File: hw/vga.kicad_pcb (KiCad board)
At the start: 2 copper layers, 36.8 x 36.8 mm, 23 parts, among them P1 CONN_01X15, P2 COLOR_SELECT, P3 CONN_01X14, P4 CONN_01X02, P5 CLOCK_SELECT, U1 74HC4053, U2 23LCV512, U3 NB3N502, Y1 10MHz

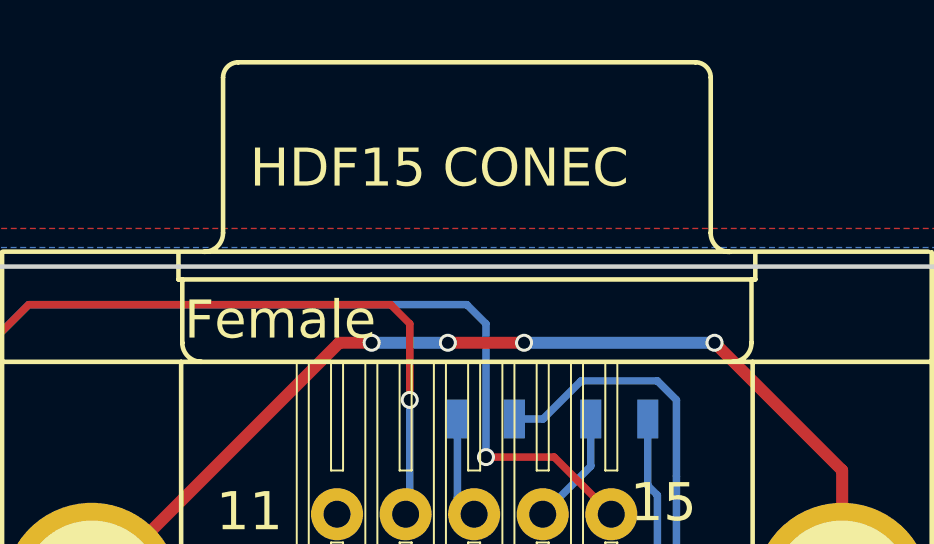
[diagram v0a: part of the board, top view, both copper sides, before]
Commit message: Upgraded project to Kicad 6
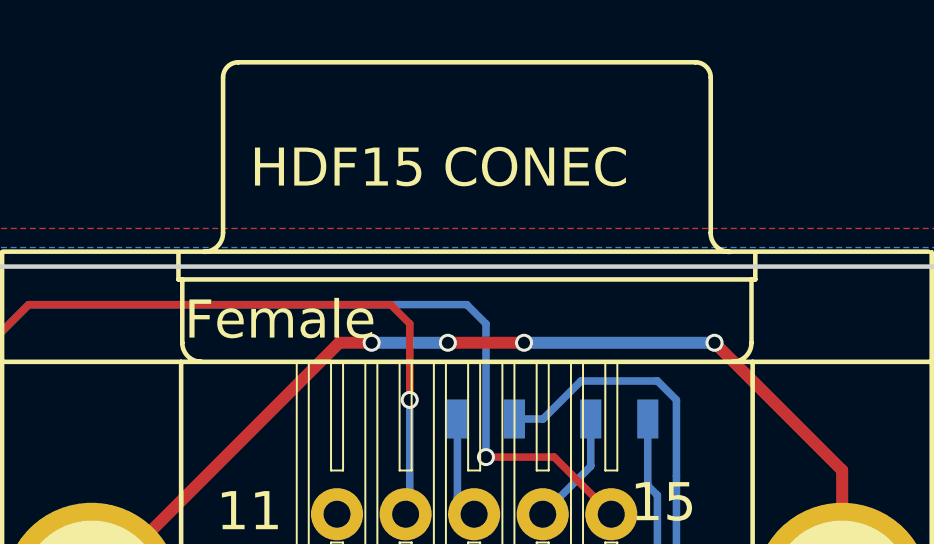
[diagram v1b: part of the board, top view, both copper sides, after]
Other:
- net class Default removed
- net class Power removed

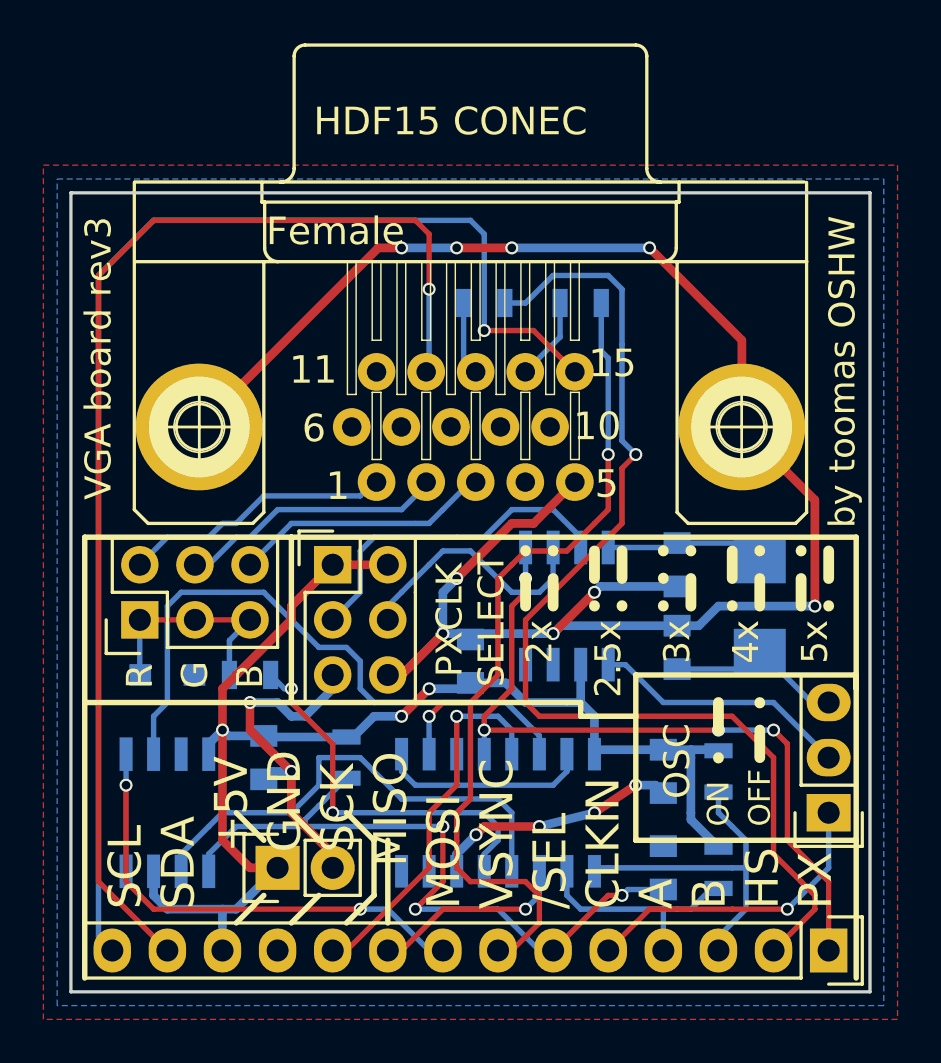
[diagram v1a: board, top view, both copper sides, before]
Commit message: Changed PLL chip to ICS501 and removed onboard oscillator option. Changed J1 footprint to 14 pin double row pin header. Swapped J1 pins 2 and 3 (hsync and B). J1 pin 1 is now ground (used to be pixel clock out). B line now has pulldown (used to be pullup). Rerouted the board for lower EMC (but still 2 layers).
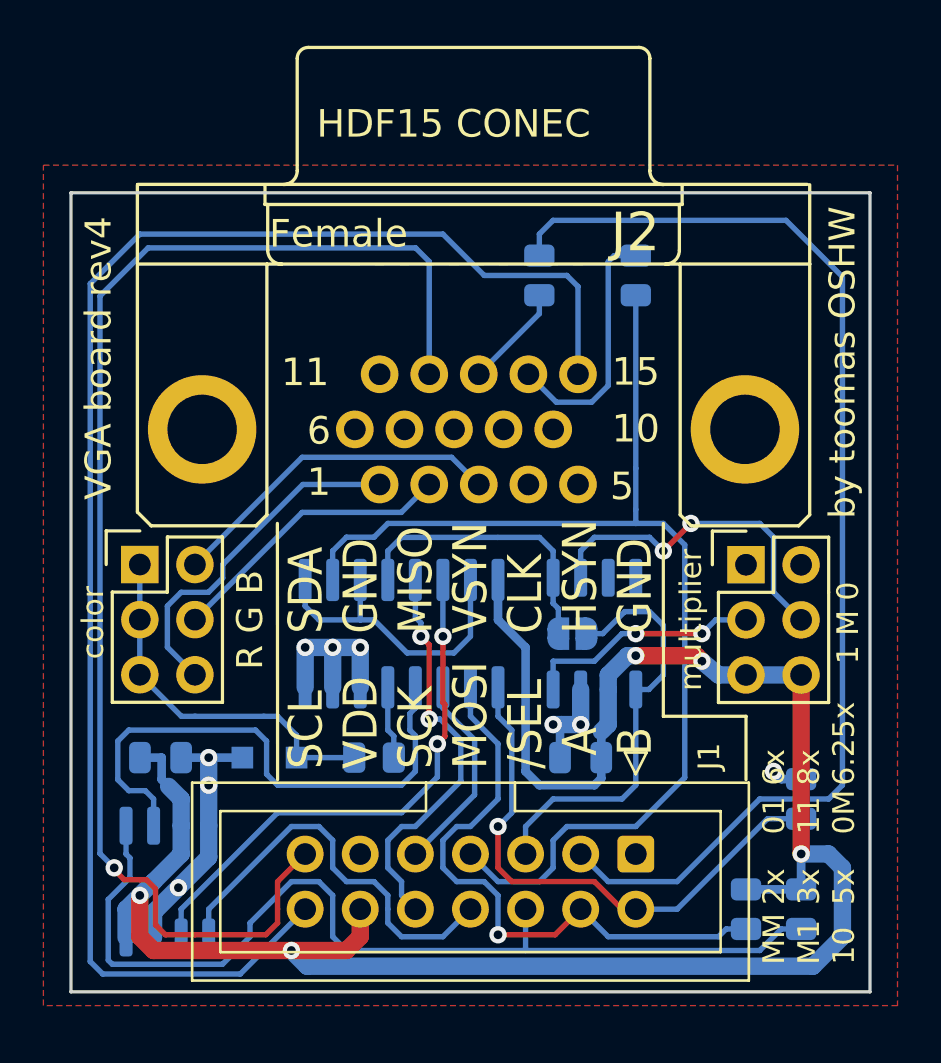
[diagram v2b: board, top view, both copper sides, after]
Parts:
- removed the C1 at (152.4, 88.3)
- removed the C2 at (161.9, 87.6)
- removed C3: 1p, Capacitors_SMD:C_0805
- removed C6: 100p, Capacitors_SMD:C_0805
- removed the JP2 at (168.9, 95.2)
- removed P1: CONN_01X15, vga:con-subd-HDF15H
- removed P3: CONN_01X14, Pin_Headers:Pin_Header_Straight_1x14
- removed P4: CONN_01X02, Pin_Headers:Pin_Header_Straight_1x02
- removed Y1: 10MHz, Crystals:Crystal_SMD_5032_2Pads
- added J1: Conn_02x07_Odd_Even, Connector_IDC:IDC-Header_2x07_P2.54mm_Vertical, F.Cu at (160.0, 97.2)
- added J2: DB15_Female_HighDensity_MountingHoles, vga:con-subd-HDF15H, F.Cu at (152.5, 77.6)
- added JP3: SolderJumper_2_Open, Jumper:SolderJumper-2_P1.3mm_Open_RoundedPad1.0x1.5mm, B.Cu at (157.1, 87.0)
- C1: renamed from C4; footprint Capacitors_SMD:C_0805 -> Capacitor_SMD:C_0805_2012Metric
- C2: renamed from C5; footprint Capacitors_SMD:C_0805 -> Capacitor_SMD:C_0805_2012Metric
- D1: footprint Diodes_SMD:SOD-323_HandSoldering -> Diode_SMD:D_SOD-323_HandSoldering
- JP1: renamed from P2; value COLOR_SELECT -> color
- JP2: renamed from P5; value CLOCK_SELECT -> multiplier
- R1: renamed from R4; value 2k2 -> 10k; footprint Resistors_SMD:R_0805 -> Resistor_SMD:R_0805_2012Metric
- R2, R3: value 2k2 -> 10k; footprint Resistors_SMD:R_0805 -> Resistor_SMD:R_0805_2012Metric
- R4: renamed from R8; footprint Resistors_SMD:R_0805 -> Resistor_SMD:R_0805_2012Metric
- R5, R6: footprint Resistors_SMD:R_0805 -> Resistor_SMD:R_0805_2012Metric
- U1: footprint Housings_SOIC:SOIC-16_3.9x9.9mm_Pitch1.27mm -> Package_SO:SOIC-16_3.9x9.9mm_P1.27mm
- U2: footprint Housings_SOIC:SOIC-8_3.9x4.9mm_Pitch1.27mm -> Package_SO:SO-8_3.9x4.9mm_P1.27mm
- U3: value NB3N502 -> ICS501; footprint Housings_SOIC:SOIC-8_3.9x4.9mm_Pitch1.27mm -> Package_SO:SO-8_3.9x4.9mm_P1.27mm
- moved R1 22.1 mm to (167.6, 99.7)
- moved JP2 19.0 mm to (165.1, 83.8)
- moved U1 9.38 mm to (149.2, 87.0)
- moved R6 6.87 mm to (148.0, 92.7)
- moved D1 6.05 mm to (143.1, 92.7), turned to 0 degrees
- moved C2 4.76 mm to (138.1, 92.7), turned to 0 degrees
- moved R2 4.02 mm to (167.6, 94.6), turned to -90 degrees
- moved C1 3.86 mm to (157.5, 92.7), turned to 180 degrees
- moved U2 3.17 mm to (138.4, 98.4), turned to -90 degrees
- moved R5 2.84 mm to (160.0, 70.5), turned to -90 degrees
- moved R4 2.84 mm to (155.6, 70.5), turned to 90 degrees
- moved JP1 2.55 mm to (137.2, 83.8), turned to 0 degrees
- moved R3 2.29 mm to (165.1, 99.7)
- moved U3 1.80 mm to (158.1, 87.0)
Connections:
- net //SEL renamed //SEL
- net /PXCLK renamed Net-(JP3-Pad2)
- JP1 pad 2: /PX_R -> /PX_B
- JP1 pad 6: /PX_B -> /PX_R
- JP2 pad 1: VDD -> GND
- JP2 pad 2: VDD -> GND
- JP2 pad 3: Net-(P5-Pad3) -> Net-(JP2-Pad3)
- JP2 pad 5: GND -> VDD
- JP2 pad 6: GND -> VDD
- R2 pad 1: /B -> GND
- R2 pad 2: VDD -> /B
- U3 pad 1: Net-(JP2-Pad2) -> /CLKIN
- U3 pad 4: Net-(U3-Pad4) -> Net-(JP2-Pad3)
- U3 pad 7: Net-(P5-Pad3) -> unconnected-(U3-Pad7)
- U3 pad 8: Net-(C3-Pad1) -> unconnected-(U3-Pad8)
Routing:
- net GND: track 108.9 -> 26.1 mm, vias 15 -> 9
- net VDD: track 66.0 -> 96.3 mm, vias 3 -> 5
- net Net-(JP3-Pad2): track 35.3 -> 13.4 mm, vias 4 -> 0
- net /A: track 10.7 -> 27.7 mm, vias 0 -> 1
- net Net-(P5-Pad3): track 16.9 -> 0.00 mm
- net /PIXEL: track 17.9 -> 3.35 mm, vias 2 -> 0
- net Net-(JP2-Pad2): track 11.9 -> 0.00 mm
- net //SEL: track 33.5 -> 45.4 mm, vias 3 -> 0
- net /SCL: track 59.9 -> 71.1 mm, vias 1 -> 0
- net Net-(JP2-Pad3): track 0.00 -> 11.0 mm, vias 0 -> 2
- net /VSYNC: track 42.1 -> 52.9 mm, vias 2 -> 0
- net /B: track 15.4 -> 25.3 mm, vias 0 -> 1
- net Net-(C2-Pad1): track 8.33 -> 0.00 mm
- net /VSYNC_OUT: track 3.84 -> 11.6 mm
- net Net-(C3-Pad1): track 7.42 -> 0.00 mm
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- removed copper zone on B.Cu, net GND
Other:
- board text added: "01 11 0M"
- board text added: "1 M 0"
- board text added: "2x 3x 5x"
- board text added: "6x 8x 6.25x"
- board text added: "MM M1 10"
- board text added: "R G B"
- board text added: "SCL VDD SCK MOSI /SEL A B"
- board text added: "SDA GND MISO VSYN CLK HSYN GND"
- board text added: "VGA board rev4"
- board text added: "color"
- board text added: "multiplier"
- board text removed: "2.5x"
- board text removed: "2x"
- board text removed: "3x"
- board text removed: "4x"
- board text removed: "5x"
- board text removed: "B"
- board text removed: "G"
- board text removed: "OFF"
- board text removed: "ON"
- board text removed: "OSC"
- board text removed: "PXCLK SELECT"
- board text removed: "R"
- board text removed: "SCL SDA +5V GND SCK MISO MOSI VSYNC /SEL CLKIN A B HS PX"
- board text removed: "VGA board rev3"

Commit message: Reduced J1 to 10pins by removing all non-essential pins. Reviewed comments on the schematic. Added solder jumper so that more PLL chips could be used. Changed AB input to use pullups like rev3 did (but with 4x higher value). Finished board layout.
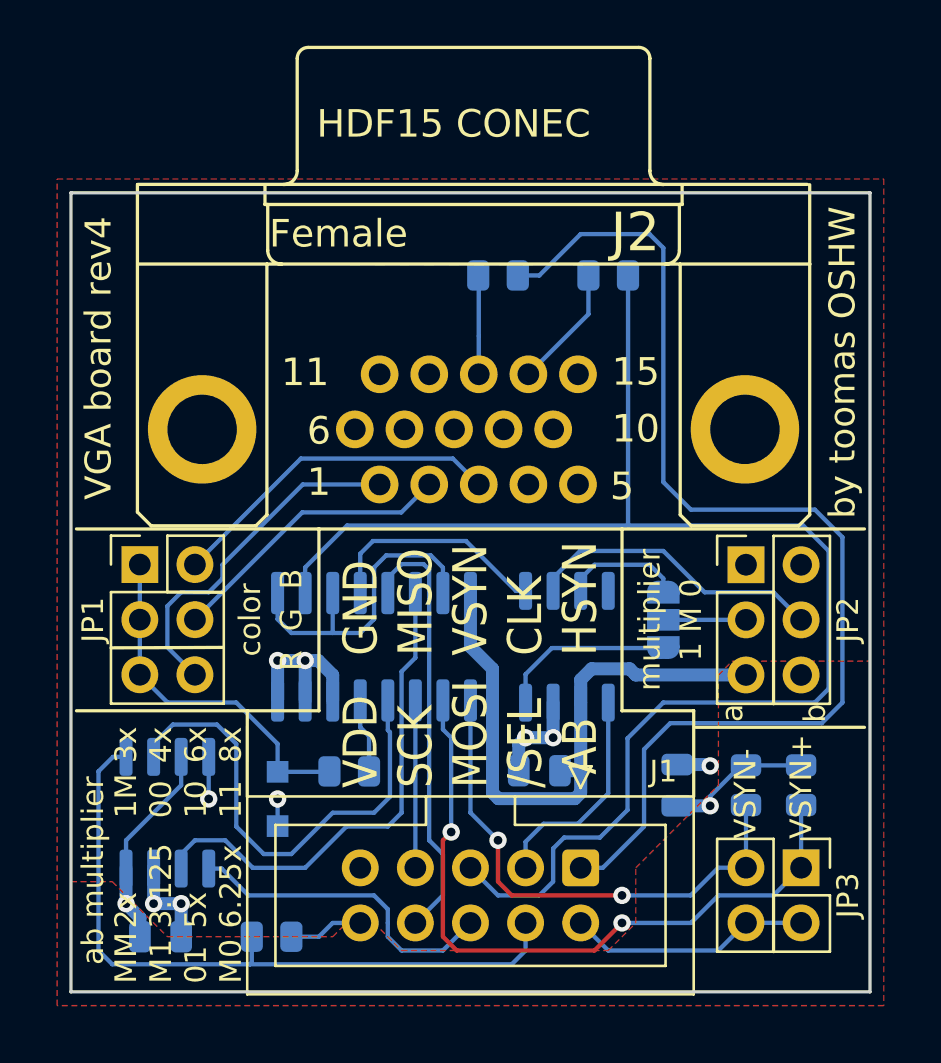
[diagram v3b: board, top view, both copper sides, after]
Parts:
- added C3: 100n, Capacitor_SMD:C_0805_2012Metric, B.Cu at (161.9, 94.0)
- added JP4: SolderJumper_3_Bridged12, Jumper:SolderJumper-3_P1.3mm_Open_RoundedPad1.0x1.5mm, B.Cu at (161.3, 86.4)
- J1: value Conn_02x07_Odd_Even -> Conn_02x05_Odd_Even; footprint Connector_IDC:IDC-Header_2x07_P2.54mm_Vertical -> Connector_IDC:IDC-Header_2x05_P2.54mm_Vertical
- JP1, JP2: footprint Pin_Headers:Pin_Header_Straight_2x03 -> Connector_PinHeader_2.54mm:PinHeader_2x03_P2.54mm_Vertical
- JP3: value SolderJumper_2_Open -> Conn_02x02_Odd_Even; footprint Jumper:SolderJumper-2_P1.3mm_Open_RoundedPad1.0x1.5mm -> Connector_PinHeader_2.54mm:PinHeader_2x02_P2.54mm_Vertical; moved to F.Cu
- moved R1 24.4 mm to (143.2, 101.0), turned to 0 degrees
- moved JP3 15.1 mm to (167.6, 97.8), turned to -90 degrees
- moved C2 8.26 mm to (138.1, 101.0)
- moved R3 5.71 mm to (165.1, 94.0), turned to -90 degrees
- moved U2 3.17 mm to (138.4, 95.2)
- moved J1 2.62 mm to (157.5, 97.8)
- moved C1 2.00 mm to (155.6, 93.3)
- moved D1 1.94 mm to (143.5, 94.6), turned to 90 degrees
- moved R4 1.91 mm to (153.7, 70.5), turned to 0 degrees
- moved U3 1.41 mm to (156.8, 87.6)
- moved U1 1.41 mm to (148.0, 87.6)
- moved R6 1.31 mm to (146.8, 93.3)
- moved R5 1.27 mm to (158.8, 70.5), turned to 0 degrees
- moved R2 0.63 mm to (167.6, 94.0)
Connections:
- net Net-(JP2-Pad4) renamed /S0_a
- J1 pad 1: GND -> /HSYNC
- J1 pad 10: /SCK -> VDD
- J1 pad 2: /B -> /AB
- J1 pad 3: /HSYNC -> /CLKIN
- J1 pad 4: /A -> //SEL
- J1 pad 5: /CLKIN -> /VSYNC
- J1 pad 6: //SEL -> /MOSI
- J1 pad 7: /VSYNC -> /MISO
- J1 pad 8: /MOSI -> /SCK
- J1 pad 9: /MISO -> GND
- J2 pad 12: /SDA -> unconnected-(J2-Pad12)
- J2 pad 15: /SCL -> unconnected-(J2-Pad15)
- JP2 pad 3: Net-(JP2-Pad3) -> /S1_b
- JP3 pad 1: /CLKIN -> Net-(JP3-Pad1)
- JP3 pad 2: Net-(JP3-Pad2) -> /AB
- R2 pad 1: GND -> VDD
- R2 pad 2: /B -> Net-(JP3-Pad1)
- R3 pad 1: /A -> VDD
- R3 pad 2: VDD -> Net-(JP3-Pad3)
- U1 pad 1: /B -> Net-(JP3-Pad3)
- U1 pad 12: Net-(JP3-Pad2) -> /PXCLK
- U1 pad 2: /A -> Net-(JP3-Pad1)
- U3 pad 4: Net-(JP2-Pad3) -> Net-(JP4-Pad1)
- U3 pad 5: Net-(JP3-Pad2) -> /PXCLK
- U3 pad 7: unconnected-(U3-Pad7) -> Net-(JP4-Pad3)
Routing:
- net /SCL: track 71.1 -> 0.00 mm
- net /SDA: track 61.9 -> 0.00 mm, vias 1 -> 0
- net VDD: track 96.3 -> 47.8 mm, vias 5 -> 2
- net Net-(JP3-Pad1): track 0.00 -> 32.5 mm, vias 0 -> 2
- net /A: track 27.7 -> 0.00 mm, vias 1 -> 0
- net /B: track 25.3 -> 0.00 mm, vias 1 -> 0
- net Net-(JP3-Pad3): track 0.00 -> 24.0 mm, vias 0 -> 2
- net /VSYNC: track 52.9 -> 68.9 mm
- net Net-(JP3-Pad2): track 13.4 -> 0.00 mm
- net //SEL: track 45.4 -> 32.6 mm
- net /AB: track 0.00 -> 11.2 mm
- net Net-(JP2-Pad3): track 11.0 -> 0.00 mm, vias 2 -> 0
- net /PXCLK: track 0.00 -> 10.6 mm
- net /CLKIN: track 19.6 -> 10.1 mm
- net Net-(JP4-Pad1): track 0.00 -> 8.16 mm
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- added copper zone on F.Cu, net VDD
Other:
- board text added: "1M 00 10 11"
- board text added: "2x 3.125 5x 6.25x"
- board text added: "3x 4x 6x 8x"
- board text added: "GND MISO VSYN CLK HSYN"
- board text added: "MM M1 01 M0"
- board text added: "VDD SCK MOSI /SEL AB"
- board text added: "VSYN+"
- board text added: "VSYN-"
- board text added: "a"
- board text added: "ab multiplier"
- board text added: "b"
- board text removed: "01 11 0M"
- board text removed: "2x 3x 5x"
- board text removed: "6x 8x 6.25x"
- board text removed: "MM M1 10"
- board text removed: "SCL VDD SCK MOSI /SEL A B"
- board text removed: "SDA GND MISO VSYN CLK HSYN GND"

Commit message: Finalized rev4 board. Added post PCB manufacturing TODOs to schematic.
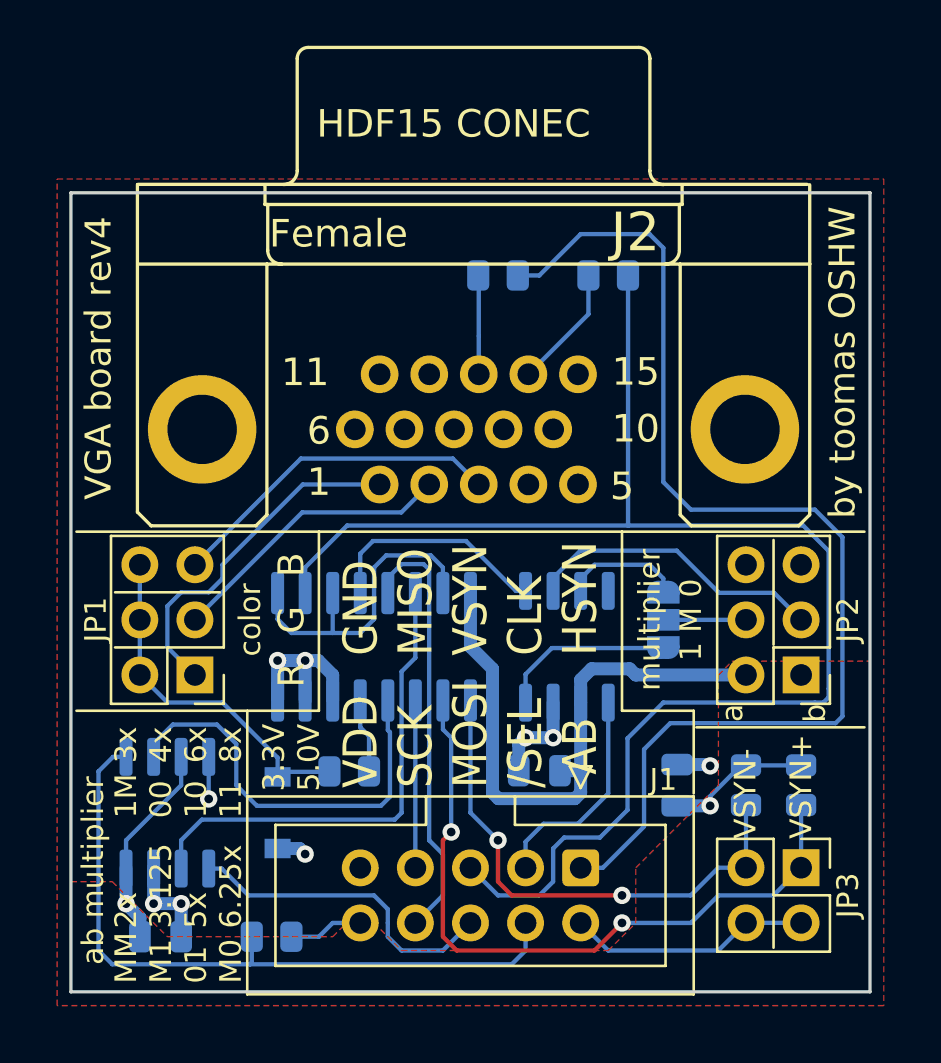
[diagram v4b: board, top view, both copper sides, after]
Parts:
- D1: footprint Diode_SMD:D_SOD-323_HandSoldering -> Diode_SMD:D_SOD-123
- moved JP1 5.69 mm to (139.7, 88.9), turned to 180 degrees
- moved JP2 5.68 mm to (167.6, 88.9), turned to 180 degrees
- moved D1 0.64 mm to (143.5, 95.2)
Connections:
- JP1 pad 1: Net-(D1-Pad2) -> /PX_R
- JP1 pad 2: /PX_B -> Net-(D1-Pad2)
- JP1 pad 3: Net-(D1-Pad2) -> /PX_G
- JP1 pad 4: /PX_G -> Net-(D1-Pad2)
- JP1 pad 5: Net-(D1-Pad2) -> /PX_B
- JP1 pad 6: /PX_R -> Net-(D1-Pad2)
- JP2 pad 1: GND -> VDD
- JP2 pad 2: GND -> VDD
- JP2 pad 3: /S1_b -> /S0_a
- JP2 pad 4: /S0_a -> /S1_b
- JP2 pad 5: VDD -> GND
- JP2 pad 6: VDD -> GND
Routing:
- net Net-(U1-Pad4): track 22.1 -> 19.2 mm
- net Net-(U1-Pad14): track 23.1 -> 22.4 mm
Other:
- board text added: "3.3V 5.0V"
- board text added: "B"
- board text added: "G"
- board text added: "R"
- board text removed: "R G B"
